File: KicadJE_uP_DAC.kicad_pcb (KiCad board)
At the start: 2 copper layers, 100 x 100 mm, 216 parts, among them J201 CV1, J202 CV2, J203 OUT1, J204 OUT2, J205 IN1, J206 IN2, J301 AVR-ISP-6, J302 UART, J401 CV1, J402 CV2, J403 OUT1, J404 OUT2, J405 OUT3, J406 OUT4, J407 IN1, J408 IN2, J409 I2C, J501 BOOT, J502 UART, J503 USB_B_Micro, P201 Doepfer_Power_16pin, P401 Doepfer_Power_16pin, SW201 SW_SPDT, SW401 SW_SPDT, U201 TL072, U202 MCP4822, U301 ATmega32A-AU, U401 TL072, U402 TL072, U405 MCP4822, U501 AMS1117-3.3, U502 STM32F103C8Tx, Y301 16MHz, Y501 8 MHz

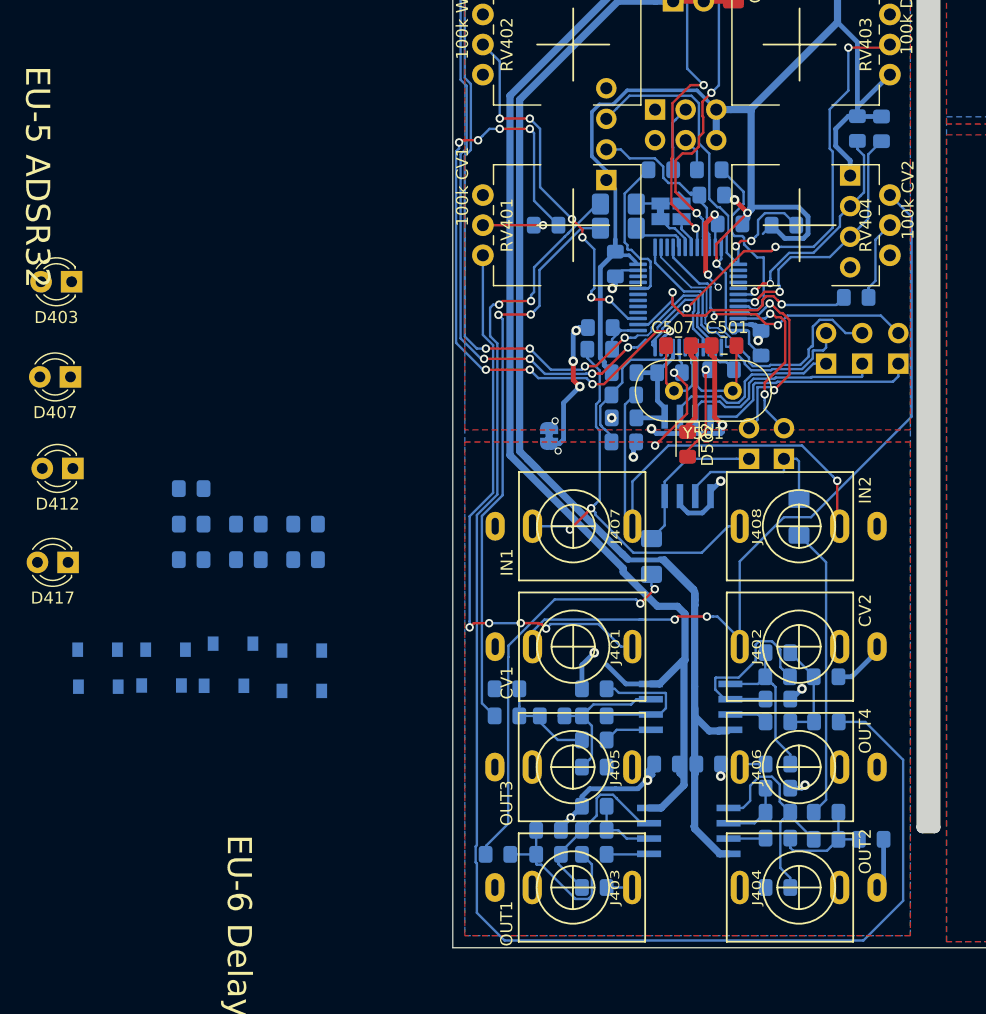
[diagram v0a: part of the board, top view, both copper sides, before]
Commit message: Diode protection - STM32
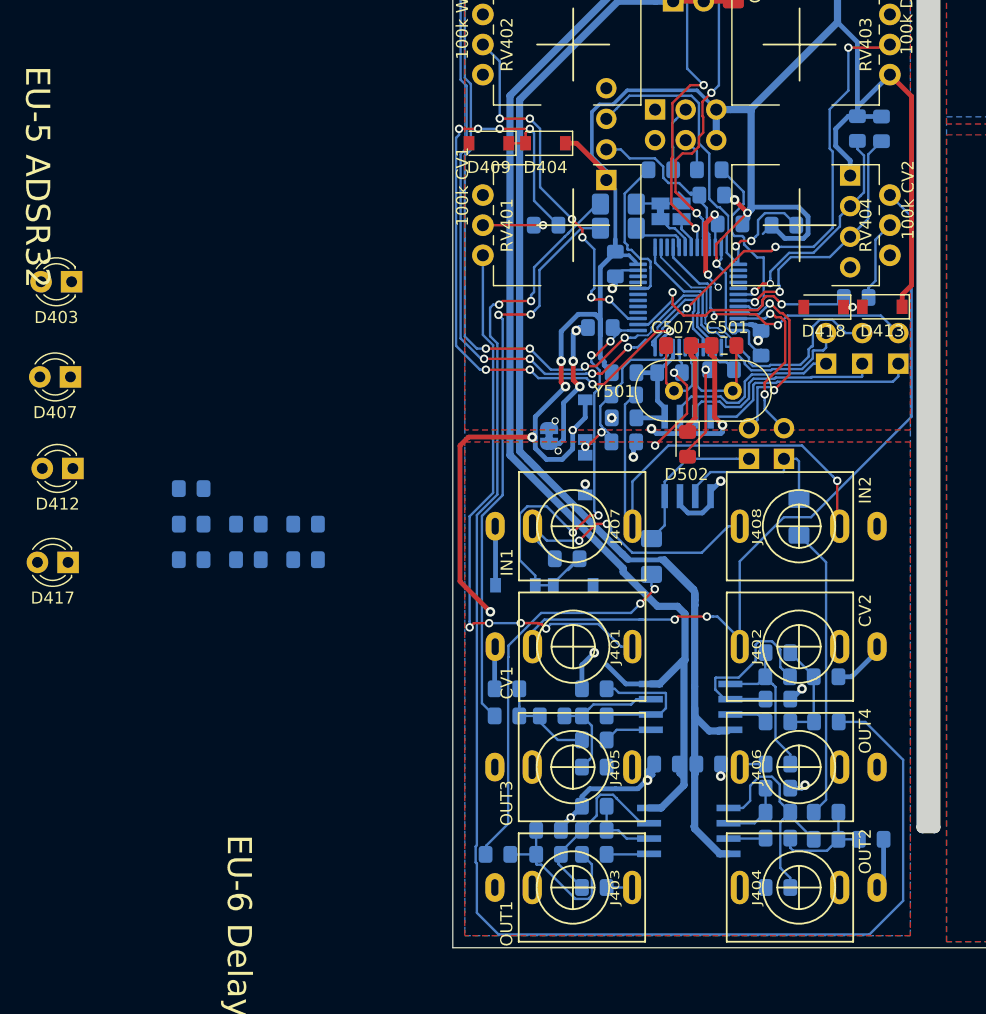
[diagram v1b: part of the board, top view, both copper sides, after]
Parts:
- D404, D409, D413, D418: moved to F.Cu
- moved D418 61.6 mm to (80.8, 96.8)
- moved D413 56.0 mm to (85.7, 96.8)
- moved D409 55.6 mm to (53.0, 83.2)
- moved D404 52.4 mm to (57.7, 83.2)
- moved D419 41.5 mm to (61.0, 106.2), turned to 270 degrees
- moved D421 39.9 mm to (60.0, 119.9)
- moved D420 32.4 mm to (61.0, 110.8), turned to 270 degrees
- moved D422 19.8 mm to (55.2, 119.9)
- moved R425 17.6 mm to (59.5, 117.7)
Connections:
- D409 pad 2: GNDA -> GND
- D418 pad 2: GNDA -> GND
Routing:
- net +3V3: track 134.1 -> 205.4 mm, vias 3 -> 8
- net STM32_IN2: track 4.07 -> 40.0 mm, vias 0 -> 4
- net Net-(J407-PadTN): track 34.8 -> 23.0 mm
- net GNDA: track 104.4 -> 113.7 mm, vias 21 -> 22
- net STM32_CV2: track 21.5 -> 25.4 mm, vias 2 -> 3
- net STM32_CV1: track 54.8 -> 58.4 mm
- net STM32_IN1: track 11.7 -> 15.2 mm, vias 0 -> 2

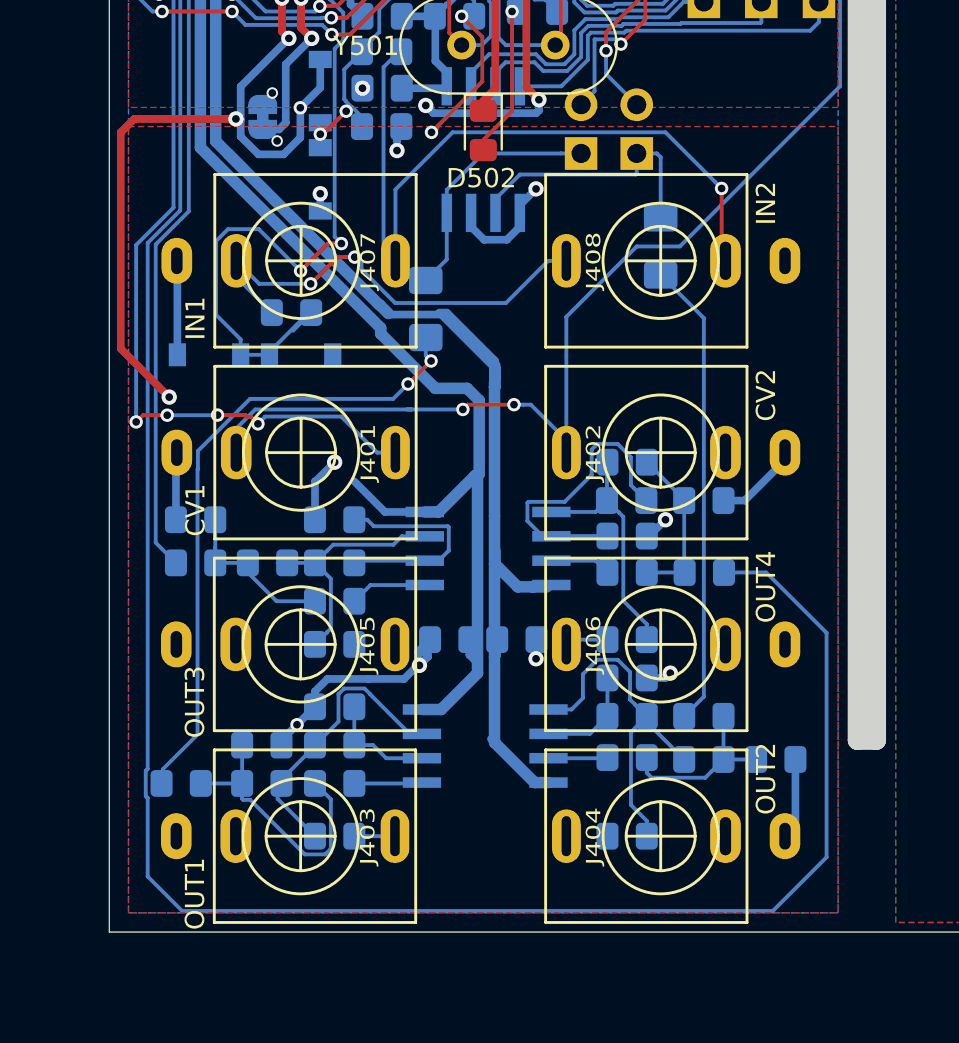
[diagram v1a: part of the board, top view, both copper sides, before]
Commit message: STM32 routed without LED's
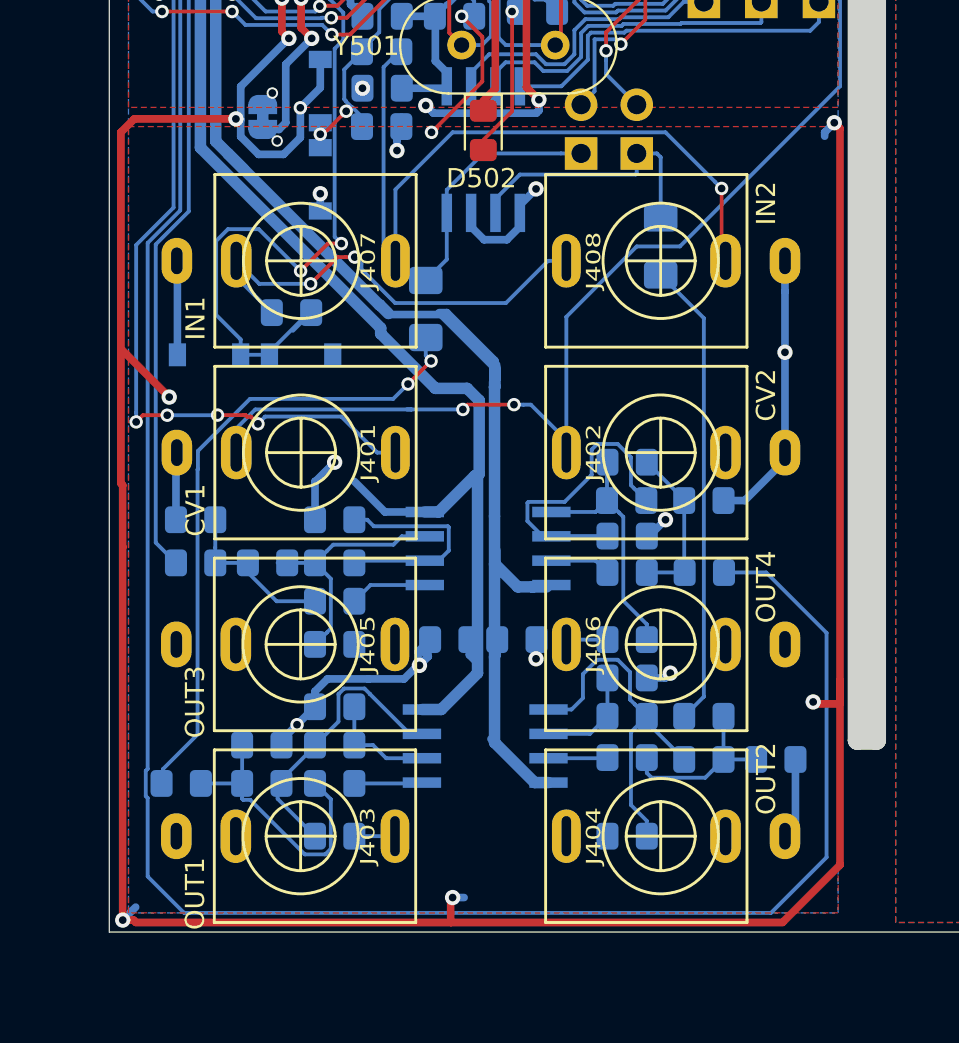
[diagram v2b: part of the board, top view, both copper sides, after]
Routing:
- net +3V3: track 205.4 -> 319.2 mm, vias 8 -> 12
- net GNDA: track 113.7 -> 123.7 mm, vias 22 -> 23
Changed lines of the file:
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@@
     (thickness 1.6)
     (drawings 39)
-    (tracks 2139)
+    (tracks 2168)
     (zones 0)
     (modules 216)
@@
   (via (at 61 111.5) (size 0.8) (drill 0.4) (layers F.Cu B.Cu) (net 4))
   (segment (start 61 112.4) (end 61 111.5) (width 0.4) (layer B.Cu) (net 4))
+  (segment (start 85.23 115) (end 85.23 116.6) (width 0.4) (layer B.Cu) (net 4))
+  (via (at 85.23 119.77) (size 0.8) (drill 0.4) (layers F.Cu B.Cu) (net 4))
+  (segment (start 85.23 119.77) (end 85.23 125) (width 0.4) (layer B.Cu) (net 4))
+  (segment (start 85.23 116.6) (end 85.23 119.77) (width 0.4) (layer B.Cu) (net 4))
   (segment (start 133.3275 73.84) (end 133.5 74.0125) (width 0.4) (layer F.Cu) (net 5) (status 30))
   (segment (start 131.29 73.84) (end 133.3275 73.84) (width 0.4) (layer F.Cu) (net 5) (status 30))
@@
   (segment (start 59.307114 90.95001) (end 59.29999 90.95001) (width 0.2) (layer B.Cu) (net 26))
   (segment (start 59.29999 90.95001) (end 56.75 93.5) (width 0.2) (layer B.Cu) (net 26))
-  (segment (start 53.355005 96.6) (end 53.849979 96.6) (width 0.2) (layer B.Cu) (net 26))
-  (segment (start 53.8 148.9) (end 52 147.1) (width 0.2) (layer B.Cu) (net 26))
-  (segment (start 84.6 148.9) (end 53.8 148.9) (width 0.2) (layer B.Cu) (net 26))
-  (segment (start 51.89999 141.592886) (end 52 141.492876) (width 0.2) (layer B.Cu) (net 26))
-  (segment (start 87.4 146.1) (end 84.6 148.9) (width 0.2) (layer B.Cu) (net 26))
-  (segment (start 87.4 134.4) (end 87.4 146.1) (width 0.2) (layer B.Cu) (net 26))
+  (segment (start 53.9 149) (end 52 147.1) (width 0.2) (layer B.Cu) (net 26))
+  (segment (start 84.5 149) (end 53.9 149) (width 0.2) (layer B.Cu) (net 26))
   (segment (start 82.05 131.25) (end 84.25 131.25) (width 0.2) (layer B.Cu) (net 26))
-  (segment (start 53.700012 99.81702) (end 53.100011 99.217019) (width 0.2) (layer B.Cu) (net 26))
+  (segment (start 87.4 146.1) (end 84.5 149) (width 0.2) (layer B.Cu) (net 26))
+  (segment (start 51.89999 141.592886) (end 52 141.492876) (width 0.2) (layer B.Cu) (net 26))
+  (segment (start 53.355005 96.6) (end 53.849979 96.6) (width 0.2) (layer B.Cu) (net 26))
   (segment (start 84.25 131.25) (end 87.4 134.4) (width 0.2) (layer B.Cu) (net 26))
-  (segment (start 53.700012 112.369351) (end 53.700012 99.81702) (width 0.2) (layer B.Cu) (net 26))
-  (segment (start 52 147.1) (end 52 143.007124) (width 0.2) (layer B.Cu) (net 26))
   (segment (start 52 143.007124) (end 51.89999 142.907114) (width 0.2) (layer B.Cu) (net 26))
+  (segment (start 87.4 134.4) (end 87.4 146.1) (width 0.2) (layer B.Cu) (net 26))
+  (segment (start 53.700012 112.369351) (end 53.700012 99.81702) (width 0.2) (layer B.Cu) (net 26))
   (segment (start 51.89999 142.907114) (end 51.89999 141.592886) (width 0.2) (layer B.Cu) (net 26))
-  (segment (start 52 114.069363) (end 53.700012 112.369351) (width 0.2) (layer B.Cu) (net 26))
   (segment (start 52 141.492876) (end 52 114.069363) (width 0.2) (layer B.Cu) (net 26))
-  (segment (start 53.100011 99.217019) (end 53.100011 96.854994) (width 0.2) (layer B.Cu) (net 26))
+  (segment (start 52 114.069363) (end 53.700012 112.369351) (width 0.2) (layer B.Cu) (net 26))
+  (segment (start 52 147.1) (end 52 143.007124) (width 0.2) (layer B.Cu) (net 26))
   (segment (start 53.100011 96.854994) (end 53.355005 96.6) (width 0.2) (layer B.Cu) (net 26))
+  (segment (start 53.700012 99.81702) (end 53.100011 99.217019) (width 0.2) (layer B.Cu) (net 26))
+  (segment (start 53.100011 99.217019) (end 53.100011 96.854994) (width 0.2) (layer B.Cu) (net 26))
   (segment (start 68.70001 91.73751) (end 68.8 91.8375) (width 0.2) (layer B.Cu) (net 27))
   (segment (start 68.70001 91.040374) (end 68.70001 91.73751) (width 0.2) (layer B.Cu) (net 27))
@@
   (segment (start 60.287019 83.2) (end 62.75 85.662981) (width 0.4) (layer F.Cu) (net 34))
   (segment (start 59.35 83.2) (end 60.287019 83.2) (width 0.4) (layer F.Cu) (net 34))
+  (via (at 50.7 149.375) (size 0.8) (drill 0.4) (layers F.Cu B.Cu) (net 34))
+  (segment (start 50.7 129.91707) (end 50.7 149.375) (width 0.4) (layer F.Cu) (net 34))
+  (segment (start 50.7 149.375) (end 51.375 148.7) (width 0.4) (layer B.Cu) (net 34))
+  (segment (start 51.265685 149.375) (end 51.390685 149.5) (width 0.4) (layer F.Cu) (net 34))
+  (segment (start 50.7 149.375) (end 51.265685 149.375) (width 0.4) (layer F.Cu) (net 34))
+  (segment (start 85.1 149.5) (end 88.09999 146.50001) (width 0.4) (layer F.Cu) (net 34))
+  (via (at 87.8 107.8) (size 0.8) (drill 0.4) (layers F.Cu B.Cu) (net 34))
+  (segment (start 88.09999 108.09999) (end 87.8 107.8) (width 0.4) (layer F.Cu) (net 34))
+  (segment (start 87.8 107.8) (end 87.3 108.3) (width 0.4) (layer B.Cu) (net 34))
+  (segment (start 87.3 108.3) (end 87.3 108.5) (width 0.4) (layer B.Cu) (net 34))
+  (via (at 67.9 148.2) (size 0.8) (drill 0.4) (layers F.Cu B.Cu) (net 34))
+  (segment (start 67.8 148.3) (end 67.9 148.2) (width 0.4) (layer F.Cu) (net 34))
+  (segment (start 67.8 149.5) (end 67.8 148.3) (width 0.4) (layer F.Cu) (net 34))
+  (segment (start 67.8 149.5) (end 85.1 149.5) (width 0.4) (layer F.Cu) (net 34))
+  (segment (start 51.390685 149.5) (end 67.8 149.5) (width 0.4) (layer F.Cu) (net 34))
+  (segment (start 67.9 148.2) (end 68.5 148.2) (width 0.4) (layer B.Cu) (net 34))
+  (segment (start 50.7 126.7) (end 50.7 129.91707) (width 0.4) (layer F.Cu) (net 34))
+  (segment (start 50.6 126.6) (end 50.7 126.7) (width 0.4) (layer F.Cu) (net 34))
+  (segment (start 50.6 119.582711) (end 50.6 126.6) (width 0.4) (layer F.Cu) (net 34))
+  (segment (start 88.09999 136.90001) (end 88.09999 138.09999) (width 0.4) (layer F.Cu) (net 34))
+  (segment (start 88.09999 136.90001) (end 88.09999 108.09999) (width 0.4) (layer F.Cu) (net 34))
+  (segment (start 88.09999 146.50001) (end 88.09999 136.90001) (width 0.4) (layer F.Cu) (net 34))
+  (via (at 86.7 138) (size 0.8) (drill 0.4) (layers F.Cu B.Cu) (net 34))
+  (segment (start 88.09999 138.09999) (end 86.79999 138.09999) (width 0.4) (layer F.Cu) (net 34))
+  (segment (start 86.79999 138.09999) (end 86.7 138) (width 0.4) (layer F.Cu) (net 34))
   (segment (start 67 102.275) (end 66.975 102.25) (width 0.4) (layer B.Cu) (net 35))
   (segment (start 67 104.58) (end 67 102.275) (width 0.4) (layer B.Cu) (net 35))

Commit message: Diode etc
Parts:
- removed D402, D403, D405, D406, D407, D410, D411, D412, D415, D416, D417: LED, LED_THT:LED_D3.0mm
- removed R429, R430, R431, R432, R433, R434: 100R, Resistor_SMD:R_0805_2012Metric_Pad1.15x1.40mm_HandSolder
- R437: value 100R -> 820R; moved to F.Cu
- moved D401 86.4 mm to (84.0, 106.0), turned to 270 degrees
- moved R437 43.9 mm to (81.0, 107.0), turned to 180 degrees
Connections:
- D401 pad 1: PB4_C0 -> GND
- D401 pad 2: PB0_R0 -> Net-(D401-Pad2)
- JP407 pad 2: /KicadJE_STM32F0/STM32F103C8/STM32_SDA1_PWM_PB9 -> PB9_PWM
- R437 pad 1: (no net) -> Net-(D401-Pad2)
- R437 pad 2: PA15_C2 -> PB9_PWM
- R506 pad 2: /KicadJE_STM32F0/STM32F103C8/STM32_boot1_PB2 -> PB2_R2
- U502 pad 20: /KicadJE_STM32F0/STM32F103C8/STM32_boot1_PB2 -> PB2_R2
- U502 pad 46: /KicadJE_STM32F0/STM32F103C8/STM32_SDA1_PWM_PB9 -> PB9_PWM
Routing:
- net GND: track 110.3 -> 179.6 mm
- net +5V: track 220.0 -> 273.6 mm, vias 4 -> 5
- net PB9_PWM: track 0.00 -> 17.1 mm, vias 0 -> 2
- net /KicadJE_STM32F0/STM32F103C8/STM32_SDA1_PWM_PB9: track 14.5 -> 0.00 mm, vias 2 -> 0
- net PB2_R2: track 0.00 -> 13.0 mm
- net /KicadJE_STM32F0/STM32F103C8/STM32_boot1_PB2: track 13.0 -> 0.00 mm
- net +3V3: track 319.2 -> 328.7 mm
- net Net-(D401-Pad2): track 0.00 -> 2.61 mm
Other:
- board text added: "DDS2"
- board text added: "Johansen Engineering STM32 - DDS2 2019 05 26"
- board text removed: "DDS 2"
- board text removed: "EU-4 Reverb"
- board text removed: "EU-5 ADSR32"
- board text removed: "Johansen Engineering ADSR Mega32 - Rev A - 2019 05 11"
- board text removed: "Johansen Engineering PT2399 - Rev B 2019 05 11"
- board text removed: "Johansen Engineering VCO3 Formant 2019 05 13"

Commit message: Before ERC Netlist
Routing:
- net /KicadJE_STM32F0/STM32F103C8/STM32_USB_P_PA12: track 38.4 -> 36.9 mm
- net GNDA: track 123.7 -> 124.8 mm
- net PWM_PA9: track 4.56 -> 3.78 mm
- net /KicadJE_STM32F0/STM32F103C8/STM32_SWDIO_PA13: track 14.3 -> 14.9 mm
